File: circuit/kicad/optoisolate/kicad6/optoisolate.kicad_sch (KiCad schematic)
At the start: 10 parts, among them J1 Power_Input, J2 MOTOR_POWER, Q1 IRF540N, U1 ATtiny85-20S, U2 AMS1117-3.3, U3 4N35

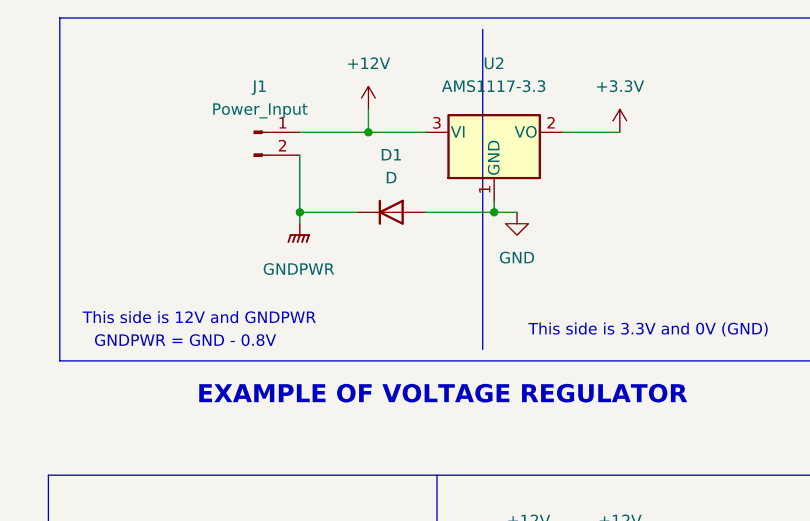
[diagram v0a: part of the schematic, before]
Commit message: OptoIsolate Example
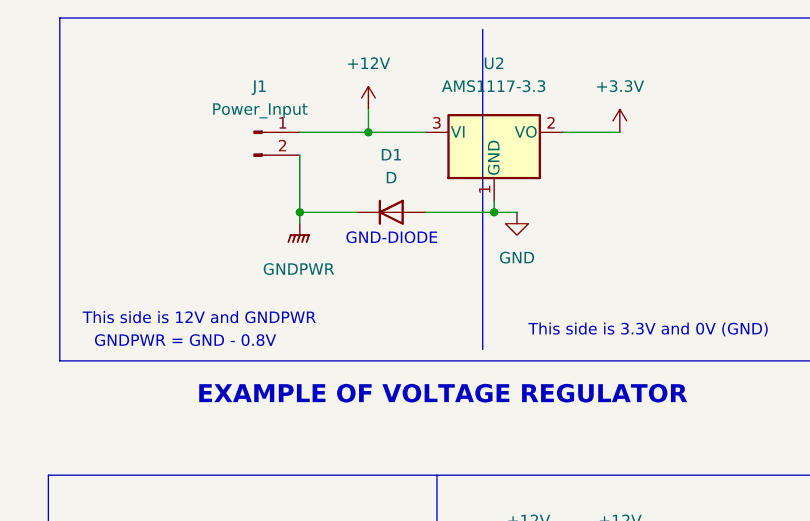
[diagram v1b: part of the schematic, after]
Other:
- note added: "GND-DIODE"
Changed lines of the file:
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@@
+    (effects (font (size 1.27 1.27)) (justify left bottom))
+  )
+  (text "GND-DIODE\n" (at 125.73 55.88 0)
     (effects (font (size 1.27 1.27)) (justify left bottom))
   )
